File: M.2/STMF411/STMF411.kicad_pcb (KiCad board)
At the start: 2 copper layers, 22 x 26 mm, 23 parts, among them M1 M.2_Key_M, Q1 2N7002, U1 LDK120PU-R_DFN6, U2 STM32F411CCUx, Y1 16 MHz

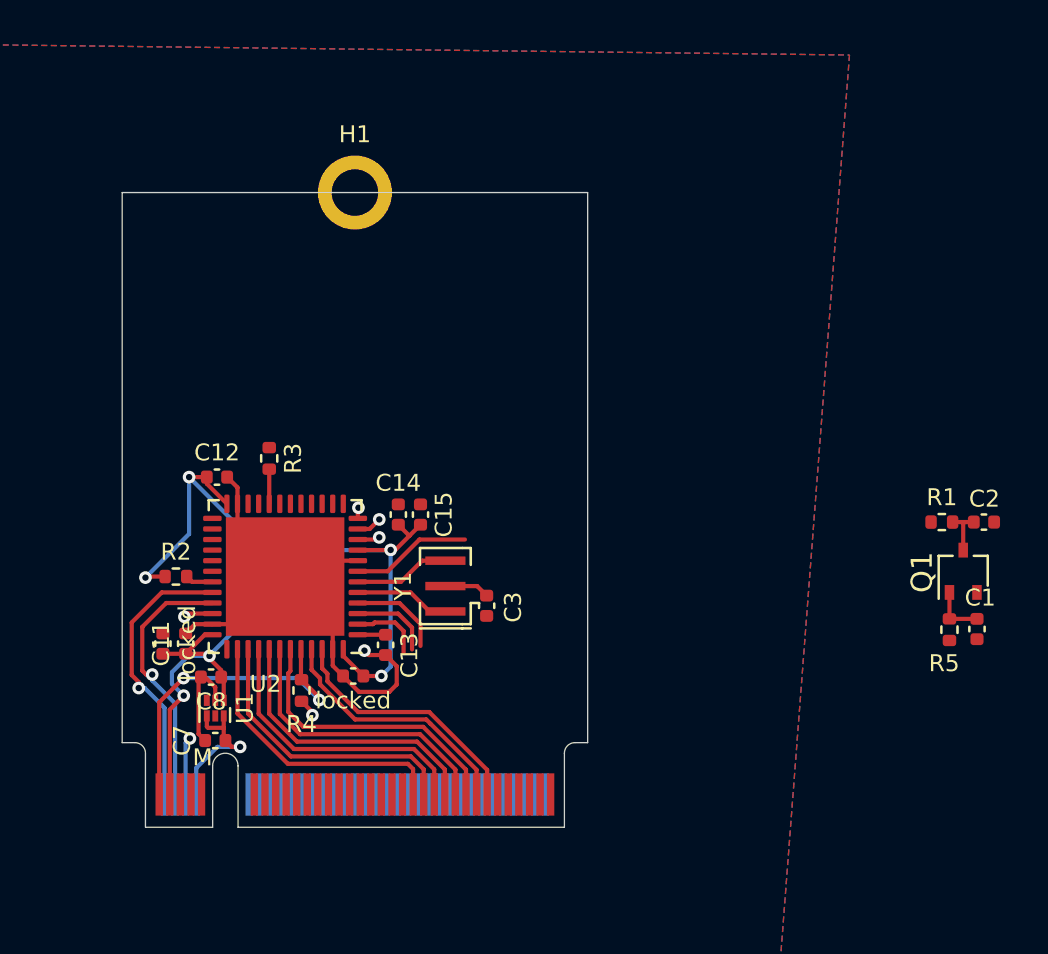
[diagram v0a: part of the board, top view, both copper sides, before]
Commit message: finish f411 and change it to key e
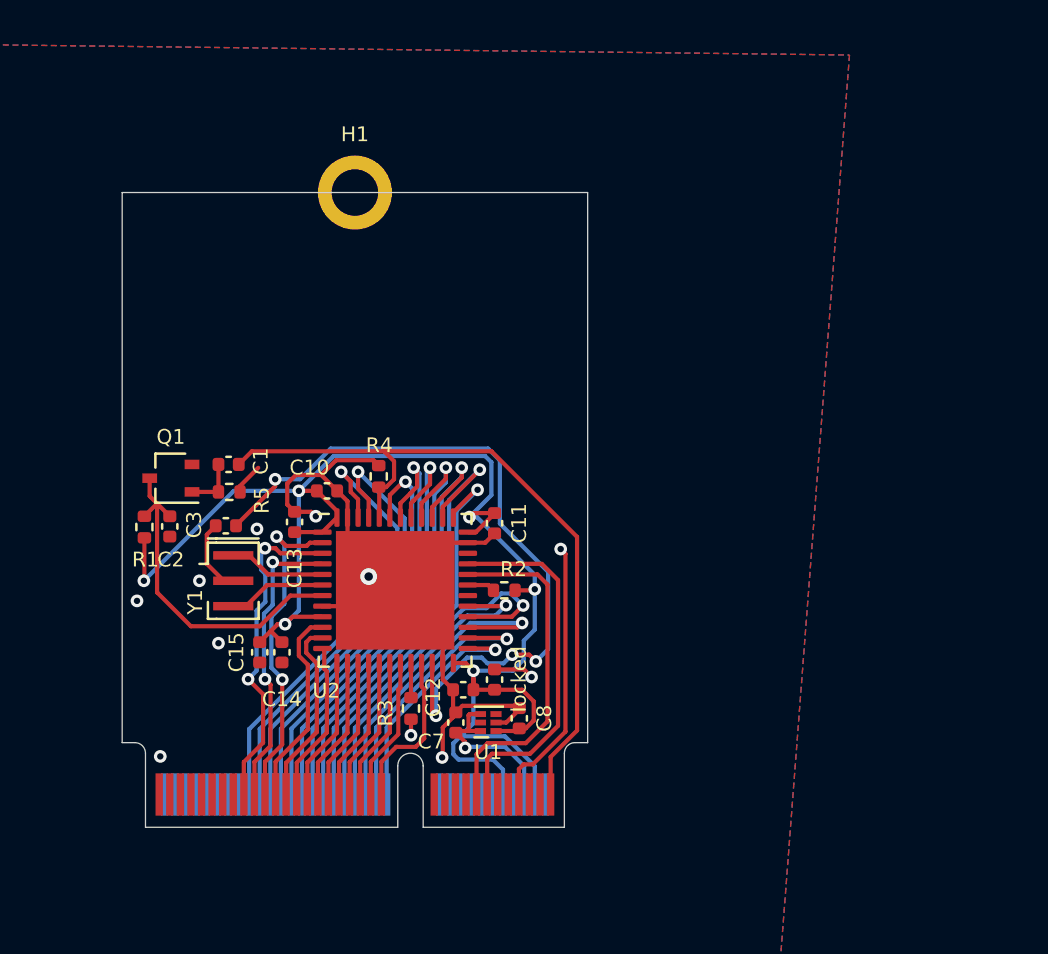
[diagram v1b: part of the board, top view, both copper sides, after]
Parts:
- M1: value M.2_Key_M -> M.2_Key_E; footprint m2ngff:m2-padKeyM -> m2ngff:m2-padKeyE
- moved C2 38.5 mm to (2.25, 15.8), turned to 90 degrees
- moved Q1 37.7 mm to (2.30, 13.5), turned to 180 degrees
- moved R1 37.7 mm to (1.05, 15.8), turned to 90 degrees
- moved C1 36.2 mm to (5.03, 12.8), turned to 0 degrees
- moved R5 34.7 mm to (5.06, 14.2), turned to 0 degrees
- moved locked 15.8 mm to (17.6, 23.0)
- moved C11 15.7 mm to (17.6, 15.6), turned to -90 degrees
- moved R2 15.5 mm to (18.1, 18.8), turned to 180 degrees
- moved C12 15.4 mm to (16.1, 23.5), turned to 180 degrees
- moved C8 14.7 mm to (18.8, 24.9), turned to 90 degrees
- moved R3 13.6 mm to (13.6, 24.4), turned to -90 degrees
- moved U1 12.9 mm to (17.3, 25.1), turned to 180 degrees
- moved C3 12.9 mm to (4.90, 15.8), turned to 180 degrees
- moved C7 11.4 mm to (15.8, 25.1), turned to 90 degrees
- moved R4 10.8 mm to (12.1, 13.4), turned to 90 degrees
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- renumbered locked to C10
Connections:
- M1 pad 1: unconnected-(M1-Pad1) -> BOOT0
- M1 pad 10: unconnected-(M1-Pad10) -> +3V3
- M1 pad 11: PC13 -> unconnected-(M1-Pad11)
- M1 pad 13: PB9 -> USB-D+
- M1 pad 14: unconnected-(M1-Pad14) -> USB-D+
- M1 pad 15: PB8 -> USB-D-
- M1 pad 16: unconnected-(M1-Pad16) -> USB-D-
- M1 pad 17: PB7 -> unconnected-(M1-Pad17)
- M1 pad 19: PB6 -> unconnected-(M1-Pad19)
- M1 pad 2: unconnected-(M1-Pad2) -> BOOT0
- M1 pad 21: PB5 -> unconnected-(M1-Pad21)
- M1 pad 23: PB4 -> unconnected-(M1-Pad23)
- M1 pad 3: unconnected-(M1-Pad3) -> +3V3
- M1 pad 32: unconnected-(M1-Pad32) -> PB12
- M1 pad 33: unconnected-(M1-Pad33) -> PB10
- M1 pad 34: unconnected-(M1-Pad34) -> PB13
- M1 pad 35: unconnected-(M1-Pad35) -> PB1
- M1 pad 36: unconnected-(M1-Pad36) -> PB14
- M1 pad 37: unconnected-(M1-Pad37) -> PB0
- M1 pad 38: unconnected-(M1-Pad38) -> PA8
- M1 pad 39: unconnected-(M1-Pad39) -> PA7
- M1 pad 4: unconnected-(M1-Pad4) -> +3V3
- M1 pad 40: unconnected-(M1-Pad40) -> PB15
- M1 pad 41: unconnected-(M1-Pad41) -> PA6
- M1 pad 42: unconnected-(M1-Pad42) -> PA14
- M1 pad 43: unconnected-(M1-Pad43) -> PA5
- M1 pad 44: unconnected-(M1-Pad44) -> PA15
- M1 pad 45: unconnected-(M1-Pad45) -> PA4
- M1 pad 46: unconnected-(M1-Pad46) -> PB3
- M1 pad 47: unconnected-(M1-Pad47) -> PA3
- M1 pad 48: unconnected-(M1-Pad48) -> PB4
- M1 pad 49: unconnected-(M1-Pad49) -> PA2
- M1 pad 5: unconnected-(M1-Pad5) -> +5V
- M1 pad 50: unconnected-(M1-Pad50) -> PB5
- M1 pad 51: unconnected-(M1-Pad51) -> PA1
- M1 pad 52: unconnected-(M1-Pad52) -> PB6
- M1 pad 53: unconnected-(M1-Pad53) -> PA0
- M1 pad 54: unconnected-(M1-Pad54) -> PB7
- M1 pad 55: unconnected-(M1-Pad55) -> PC13
- M1 pad 56: unconnected-(M1-Pad56) -> PB8
- M1 pad 57: unconnected-(M1-Pad57) -> PC15
- M1 pad 58: unconnected-(M1-Pad58) -> PB9
- M1 pad 6: unconnected-(M1-Pad6) -> +5V
- M1 pad 68: +5V -> unconnected-(M1-Pad68)
- M1 pad 7: PC15 -> GND
- M1 pad 70: GND -> unconnected-(M1-Pad70)
- M1 pad 72: USB-D+ -> unconnected-(M1-Pad72)
- M1 pad 73: +3V3 -> unconnected-(M1-Pad73)
- M1 pad 74: USB-D- -> unconnected-(M1-Pad74)
- M1 pad 75: BOOT0 -> unconnected-(M1-Pad75)
- M1 pad 8: unconnected-(M1-Pad8) -> GND
- M1 pad 9: PC14 -> +3V3
- U2 pad 34: unconnected-(U2-Pad34) -> PA13
- U2 pad 37: unconnected-(U2-Pad37) -> PA14
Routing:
- net /vcap: track 0.00 -> 34.7 mm, vias 0 -> 4
- net +3V3: track 55.9 -> 76.1 mm
- net BOOT0: track 15.6 -> 34.4 mm, vias 2 -> 0
- net PA14: track 0.00 -> 18.8 mm, vias 0 -> 1
- net PB15: track 0.00 -> 17.3 mm, vias 0 -> 1
- net PB14: track 0.00 -> 15.3 mm, vias 0 -> 1
- net PA8: track 0.00 -> 14.5 mm, vias 0 -> 1
- net PB13: track 0.00 -> 13.0 mm, vias 0 -> 1
- net PC13: track 3.40 -> 15.6 mm, vias 0 -> 2
- net PC14: track 3.87 -> 15.6 mm, vias 0 -> 2
- net PB12: track 0.00 -> 11.1 mm, vias 0 -> 1
- net PB9: track 12.1 -> 21.7 mm, vias 0 -> 1
- net PC15: track 4.41 -> 14.0 mm, vias 0 -> 2
- net PB8: track 12.1 -> 21.4 mm, vias 0 -> 1
- net PA0: track 1.05 -> 9.49 mm, vias 1 -> 0
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
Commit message: finish working on stmf411
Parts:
- added Ref**: Val**, pcbart:LogoSmall, F.Cu at (3.20, 23.5)
- H1: footprint MountingHole:MountingHole_2.2mm_M2_ISO7380_Pad -> MountingHole:MountingHole_3.2mm_M3_Pad_Via
- moved C11 0.73 mm to (17.6, 14.9)
- moved C12 0.73 mm to (16.1, 22.8)
- moved C14 0.73 mm to (7.55, 21.0)
- moved C15 0.73 mm to (6.50, 21.0)
- moved C7 0.73 mm to (15.8, 24.3)
- moved C8 0.73 mm to (18.8, 24.1)
- moved R2 0.73 mm to (18.1, 18.1)
- moved R3 0.73 mm to (13.6, 23.7)
- moved U1 0.73 mm to (17.3, 24.3)
- moved U2 0.73 mm to (12.9, 18.1)
- moved Y1 0.73 mm to (5.25, 17.6)
- moved C1 0.72 mm to (5.03, 12.1)
- moved C10 0.72 mm to (9.68, 13.4)
- moved C13 0.72 mm to (8.15, 14.8)
- moved C2 0.72 mm to (2.25, 15.1)
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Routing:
- net PC13: track 15.6 -> 18.2 mm
- net /vcap: track 34.7 -> 34.1 mm
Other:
- board text added: "MUD Project M.2 Carrierboard STMF411 Edition Designed by Pat"

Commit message: touchups to f411
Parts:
- removed Ref**: Val**, pcbart:LogoSmall
- added L1: TapTap Logo, LogoSmall:tt_4mm, F.Cu at (18.5, 3.50)
- added SW1: RESET, LogoSmall:LogoSmall, F.Cu at (3.88, 3.50)
- moved C1 4.00 mm to (5.03, 8.12)
- moved C10 4.00 mm to (9.68, 9.38)
- moved C11 4.00 mm to (17.6, 10.9)
- moved C12 4.00 mm to (16.1, 18.8)
- moved C13 4.00 mm to (8.15, 10.8)
- moved C14 4.00 mm to (7.55, 17.0)
- moved C15 4.00 mm to (6.50, 17.0)
- moved C2 4.00 mm to (2.25, 11.1)
- moved C3 4.00 mm to (4.90, 11.0)
- moved C7 4.00 mm to (15.8, 20.3)
- moved C8 4.00 mm to (18.8, 20.1)
- moved Q1 4.00 mm to (2.30, 8.78)
- moved R1 4.00 mm to (1.05, 11.1)
- moved R2 4.00 mm to (18.1, 14.1)
- moved R3 4.00 mm to (13.6, 19.7)
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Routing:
- net +3V3: track 75.7 -> 91.9 mm, vias 6 -> 7
- net GND: track 45.6 -> 55.9 mm, vias 11 -> 18
- net BOOT0: track 34.4 -> 43.4 mm
- net PC15: track 14.0 -> 19.6 mm
- net PC14: track 15.6 -> 21.2 mm
- net PC13: track 18.2 -> 23.6 mm
- net PB15: track 17.3 -> 22.0 mm
- net PA8: track 14.5 -> 19.2 mm
- net PA3: track 6.79 -> 11.5 mm
- net PB1: track 6.79 -> 11.5 mm
- net USB-D-: track 16.3 -> 21.1 mm
- net PB13: track 13.0 -> 17.7 mm
- net PA7: track 6.79 -> 11.5 mm
- net PA14: track 18.8 -> 23.5 mm
- net +5V: track 7.85 -> 12.6 mm
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
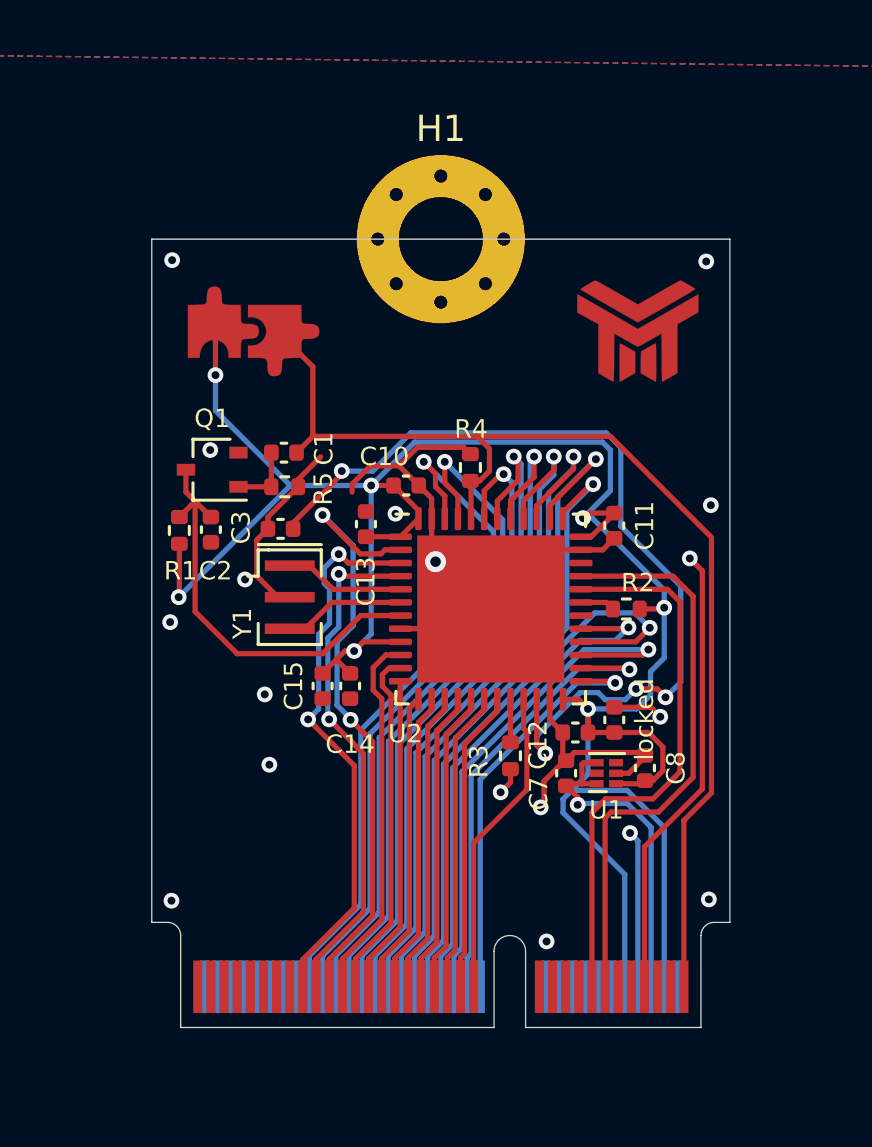
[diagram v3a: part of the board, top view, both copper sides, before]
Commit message: finalize f411 for the last time. change to sot-23 ldo
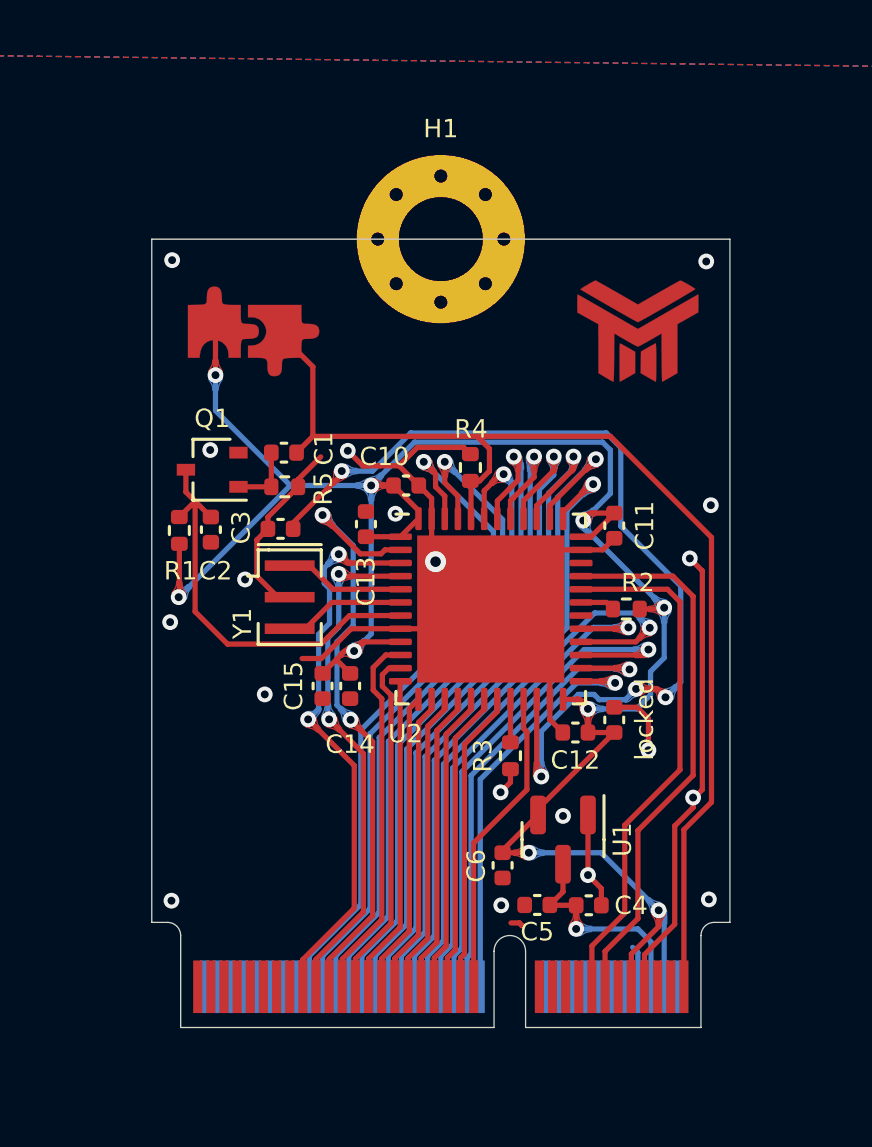
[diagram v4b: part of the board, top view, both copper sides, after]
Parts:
- removed C7, C8: 1uF, Capacitor_SMD:C_0402_1005Metric
- added C4: 4.7uF, Capacitor_SMD:C_0402_1005Metric, F.Cu at (16.6, 25.4)
- added C5: 1uF, Capacitor_SMD:C_0402_1005Metric, F.Cu at (14.7, 25.3)
- added C6: 1uF, Capacitor_SMD:C_0402_1005Metric, F.Cu at (13.3, 23.8)
- U1: value LDK120PU-R_DFN6 -> XC6206P332MR; footprint Package_DFN_QFN:DFN-6_1.3x1.2mm_P0.4mm -> Package_TO_SOT_SMD:SOT-23
- moved U1 3.02 mm to (15.7, 22.9), turned to -90 degrees
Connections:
- U1 pad 1: +3V3 -> GND
- U1 pad 2: GND -> +3V3
- U1 pad 3: unconnected-(U1-Pad3) -> +5V
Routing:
- net +3V3: track 91.9 -> 83.5 mm, vias 7 -> 9
- net +5V: track 12.6 -> 8.40 mm
- net GND: track 55.9 -> 52.8 mm, vias 18 -> 19
- net /vcap: track 34.1 -> 35.5 mm
- net USB-D-: track 21.1 -> 20.0 mm
- net USB-D+: track 21.9 -> 20.8 mm

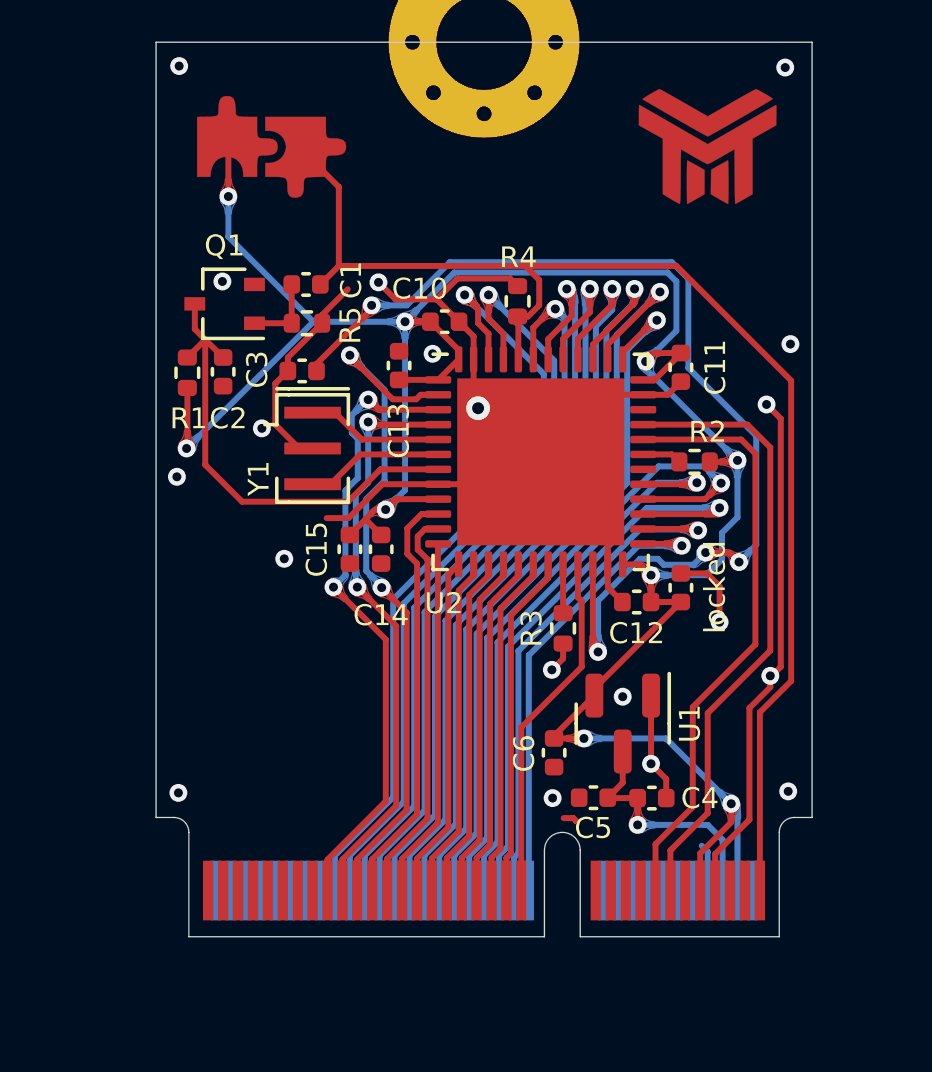
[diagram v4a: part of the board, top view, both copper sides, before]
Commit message: change stm to use 5v instead of 3.3v on vout
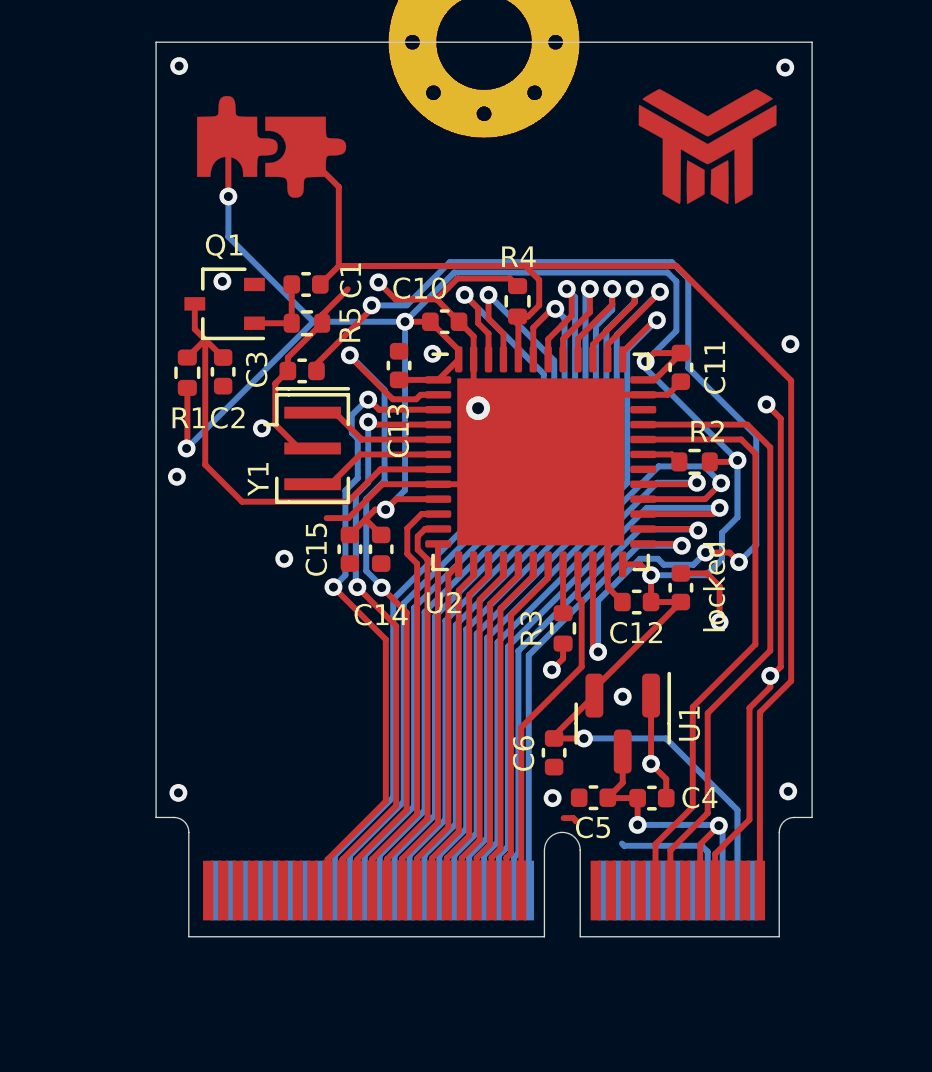
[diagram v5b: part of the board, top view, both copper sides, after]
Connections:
- M1 pad 10: +3V3 -> +5V
- M1 pad 9: +3V3 -> +5V
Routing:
- net +3V3: track 83.5 -> 80.2 mm, vias 9 -> 8
- net GND: track 52.8 -> 55.5 mm
- net +5V: track 8.40 -> 11.0 mm, vias 1 -> 2

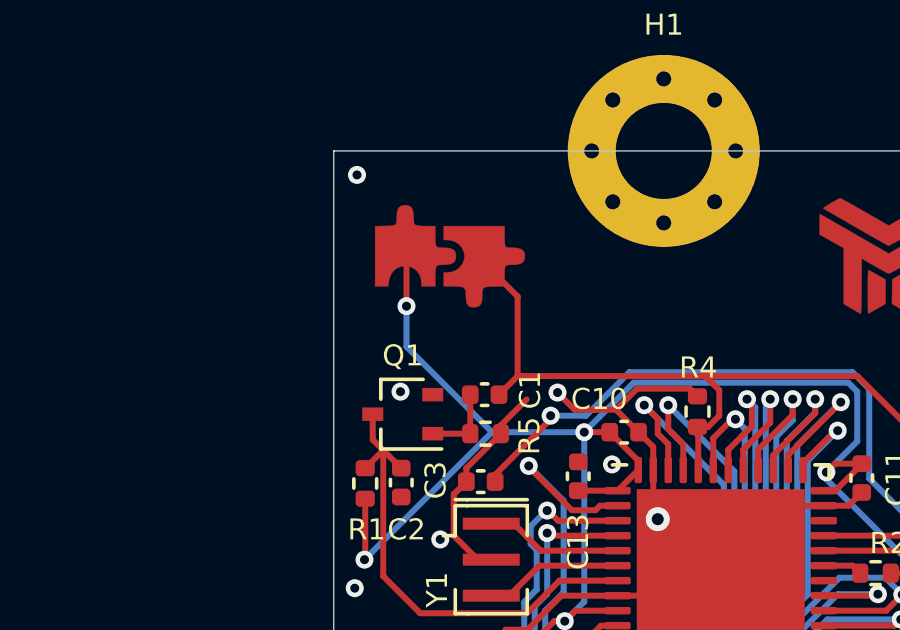
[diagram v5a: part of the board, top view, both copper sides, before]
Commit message: change modules to new logo
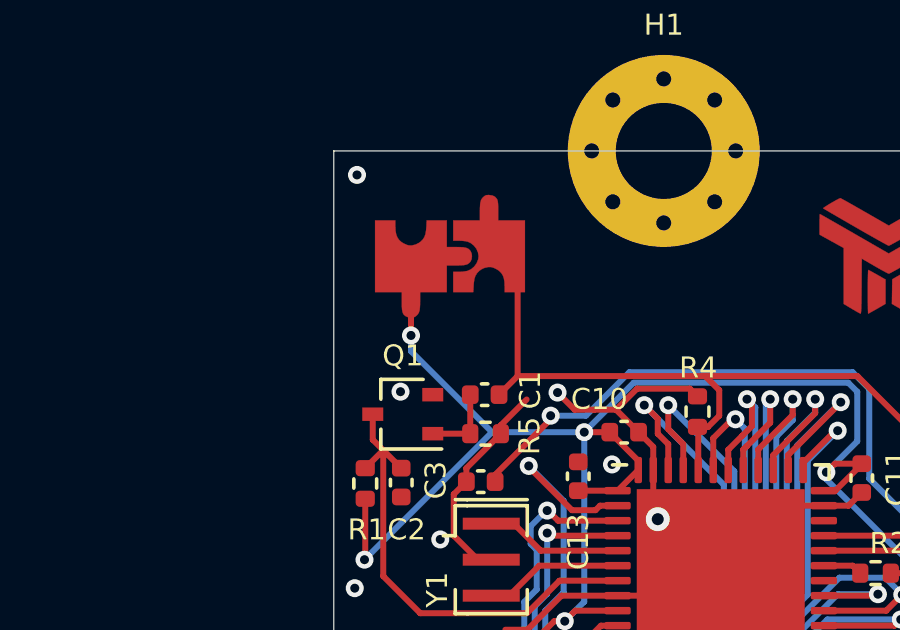
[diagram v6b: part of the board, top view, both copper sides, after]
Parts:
- SW1: footprint LogoSmall:LogoSmall -> LogoSmall:LogoSmall_Cu
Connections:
- SW1 pad 1: BOOT0 -> +3V3
- SW1 pad 2: +3V3 -> BOOT0
